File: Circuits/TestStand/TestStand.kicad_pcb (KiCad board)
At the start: 2 copper layers, 72.5 x 95 mm, 53 parts, among them J1 Screw_Terminal_01x07, J10 Screw_Terminal_01x03, J11 Screw_Terminal_01x03, J12 Screw_Terminal_01x03, J13 Screw_Terminal_01x03, J2 Screw_Terminal_01x07, J3 Screw_Terminal_01x07, J4 Screw_Terminal_01x03, J5 Screw_Terminal_01x03, J6 Screw_Terminal_01x03, J7 Screw_Terminal_01x03, J8 Screw_Terminal_01x03, J9 Screw_Terminal_01x03, Q1 MMBT4403-7-F, Q2 MMBT4403-7-F, Q3 MMBT4403-7-F, U1 HX711, U2 HX711, U3 HX711, U4 Teensy4.1

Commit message: did some traces
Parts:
- added C13: 0.01uF, Capacitor_SMD:C_0805_2012Metric, F.Cu at (98.5, 92.5)
- added C14: 10uF, Capacitor_SMD:C_0805_2012Metric, F.Cu at (92.5, 99.5)
- added C15: 10uF, Capacitor_SMD:C_0805_2012Metric, F.Cu at (92.5, 102.0)
- added C16: 33nF, Capacitor_SMD:C_0805_2012Metric, F.Cu at (71.5, 91.7)
- added C17: 22pF, Capacitor_SMD:C_0805_2012Metric, F.Cu at (85.0, 87.7)
- added C18: 22pF, Capacitor_SMD:C_0805_2012Metric, F.Cu at (85.0, 89.7)
- added C19: 2.2uF, Capacitor_SMD:C_0805_2012Metric, F.Cu at (78.0, 82.7)
- added C20: 4.7pF, Capacitor_SMD:C_0805_2012Metric, F.Cu at (78.0, 85.2)
- added C21: 1.5pF, Capacitor_SMD:C_0805_2012Metric, F.Cu at (72.5, 76.2)
- added C22: 1pF, Capacitor_SMD:C_0805_2012Metric, F.Cu at (76.0, 74.2)
- added C23: 10uF, Capacitor_SMD:C_0805_2012Metric, F.Cu at (66.5, 82.7)
- added C24: 10nF, Capacitor_SMD:C_0805_2012Metric, F.Cu at (66.5, 85.2)
- added C25: 1nF, Capacitor_SMD:C_0805_2012Metric, F.Cu at (66.5, 87.7)
- added D1: 1N4148, Diode_THT:D_DO-35_SOD27_P7.62mm_Horizontal, F.Cu at (96.5, 115.6)
- added D2: 1N4148, Diode_THT:D_DO-35_SOD27_P7.62mm_Horizontal, F.Cu at (100.0, 115.6)
- added FB1: FerriteBead, Inductor_SMD:L_0805_2012Metric, F.Cu at (97.5, 88.5)
- added FB2: FerriteBead, Inductor_SMD:L_0805_2012Metric, F.Cu at (99.5, 88.5)
- added J14: Screw_Terminal_01x02, Connector_Wago:Wago_734-132_1x02_P3.50mm_Vertical, F.Cu at (110.0, 90.0)
- added J15: Conn_Coaxial, Connector_Coaxial:SMA_Molex_73251-1153_EdgeMount_Horizontal, F.Cu at (72.5, 69.0)
- added L4: 2.7nH, Inductor_SMD:L_0805_2012Metric, F.Cu at (77.0, 79.7)
- added L5: 8.2nH, Inductor_SMD:L_0805_2012Metric, F.Cu at (76.0, 76.7)
- added L6: 3.9nH, Inductor_SMD:L_0805_2012Metric, F.Cu at (73.5, 79.1)
- added R16: 10k, Resistor_SMD:R_0805_2012Metric, F.Cu at (96.5, 105.5)
- added R17: 10k, Resistor_SMD:R_0805_2012Metric, F.Cu at (100.0, 105.5)
- added R18: 22k, Resistor_SMD:R_0805_2012Metric, F.Cu at (71.5, 87.7)
- added R19: 1M, Resistor_SMD:R_0805_2012Metric, F.Cu at (80.0, 88.8)
- added U5: LP2980IM5X-3.3/NOPB, Library:MF05A_TEX, F.Cu at (92.5, 95.7)
- added U6: MAX31855KASA, Package_SO:SOIC-8_3.9x4.9mm_P1.27mm, F.Cu at (98.5, 99.5)
- added U7: NRF24L01, Package_DFN_QFN:QFN-20-1EP_4x4mm_P0.5mm_EP2.5x2.5mm, F.Cu at (75.5, 89.6)
- added U8: LP2980IM5X-3.3/NOPB, Library:MF05A_TEX, F.Cu at (66.5, 91.4)
- added Y1: 16Mhz, Crystal:Crystal_SMD_2012-2Pin_2.0x1.2mm, F.Cu at (82.0, 88.7)
- moved J10 20.5 mm to (110.0, 145.9)
- moved J11 20.5 mm to (110.0, 131.9)
- moved J12 20.5 mm to (110.0, 118.0)
- moved J13 20.5 mm to (110.0, 104.0)
- moved J9 20.5 mm to (110.0, 160.0)
- moved J4 9.84 mm to (36.0, 168.5)
- moved J5 9.84 mm to (50.5, 168.5)
- moved J6 9.84 mm to (65.0, 168.5)
- moved J7 9.84 mm to (79.5, 168.5)
- moved J8 9.84 mm to (94.0, 168.5)
- moved U4 5.44 mm to (75.9, 130.7)
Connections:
- U4 pad 18: unconnected-(U4-26_A12_MOSI1-Pad18) -> /rMOSI
- U4 pad 19: unconnected-(U4-27_A13_SCK1-Pad19) -> /rSCK
- U4 pad 20: unconnected-(U4-28_RX7-Pad20) -> /rCE
- U4 pad 21: unconnected-(U4-29_TX7-Pad21) -> /rIRQ
- U4 pad 25: unconnected-(U4-33_MCLK2-Pad25) -> /tcCS
- U4 pad 26: unconnected-(U4-34_RX8-Pad26) -> /tcSO
- U4 pad 27: unconnected-(U4-35_TX8-Pad27) -> /tcSCK
- U4 pad 30: unconnected-(U4-38_CS1_IN1-Pad30) -> /rCSN
- U4 pad 31: unconnected-(U4-39_MISO1_OUT1A-Pad31) -> /rMISO
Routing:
- net GND: track 23.6 -> 106.7 mm, vias 4 -> 25
- net /PWM0: track 0.00 -> 62.6 mm
- net /PWM4: track 0.00 -> 56.5 mm
- net /PWM1: track 0.00 -> 54.1 mm
- net /tcSO: track 0.00 -> 52.8 mm
- net /PWM3: track 0.00 -> 52.6 mm
- net /tcCS: track 0.00 -> 49.6 mm
- net /PWM2: track 0.00 -> 45.6 mm
- net /+3VRF: track 0.00 -> 44.4 mm, vias 0 -> 2
- net /PT0: track 0.00 -> 41.0 mm
- net /B2+: track 0.00 -> 38.5 mm
- net /DAT2: track 0.00 -> 37.1 mm
- net /B1+: track 0.00 -> 37.0 mm
- net /SCK2: track 0.00 -> 36.0 mm
- net /PT1: track 0.00 -> 33.3 mm
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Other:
- board size 72.5 x 95 mm -> 92.5 x 111 mm

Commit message: added glow plug circuitry to schematic
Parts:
- added IC1: STP85NF55, Library:TO255P460X1020X2008-3P, F.Cu at (152.1, 96.5)
- added J16: Screw_Terminal_01x02, Connector_Wago:Wago_734-132_1x02_P3.50mm_Vertical, F.Cu at (152.5, 104.0)
- added R20: 10K, Resistor_SMD:R_0805_2012Metric, F.Cu at (158.5, 115.0)
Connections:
- U4 pad 13: unconnected-(U4-11_MOSI_CTX1-Pad13) -> /GP

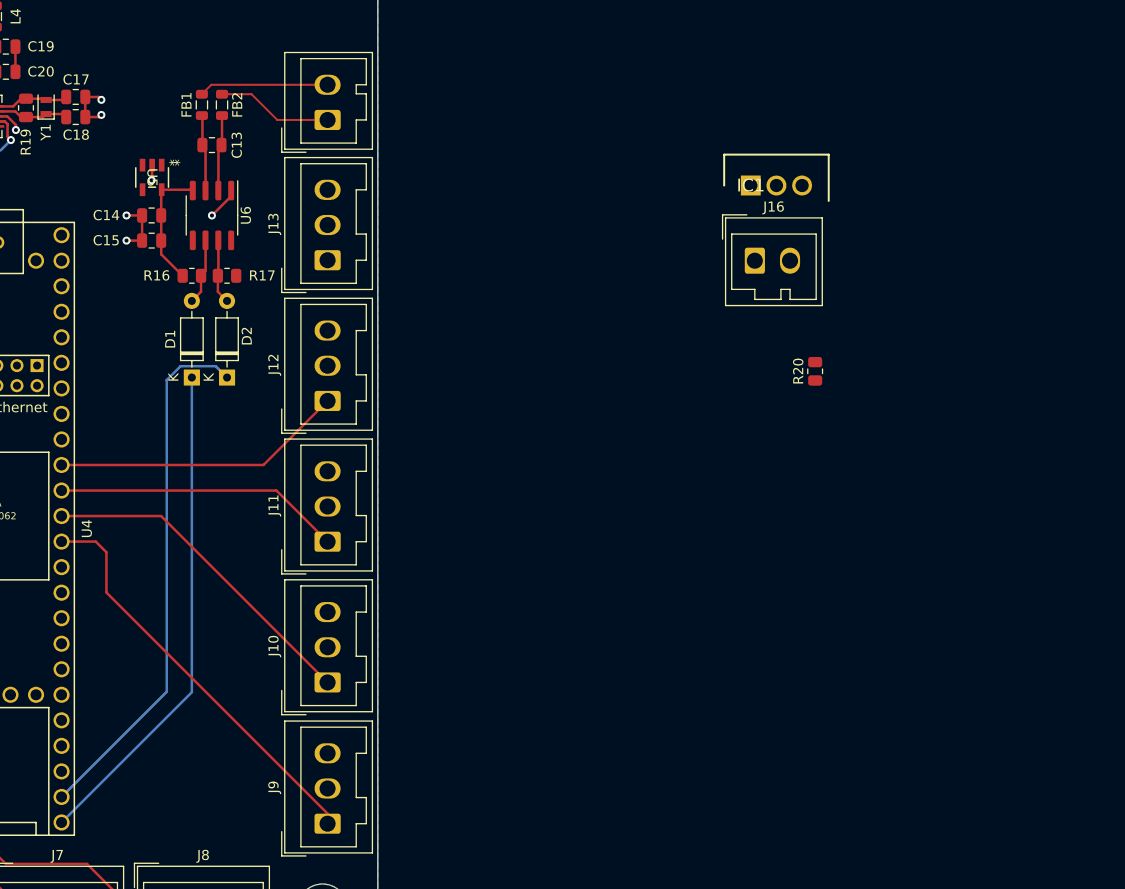
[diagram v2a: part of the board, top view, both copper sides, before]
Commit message: added voltage regulator stuff
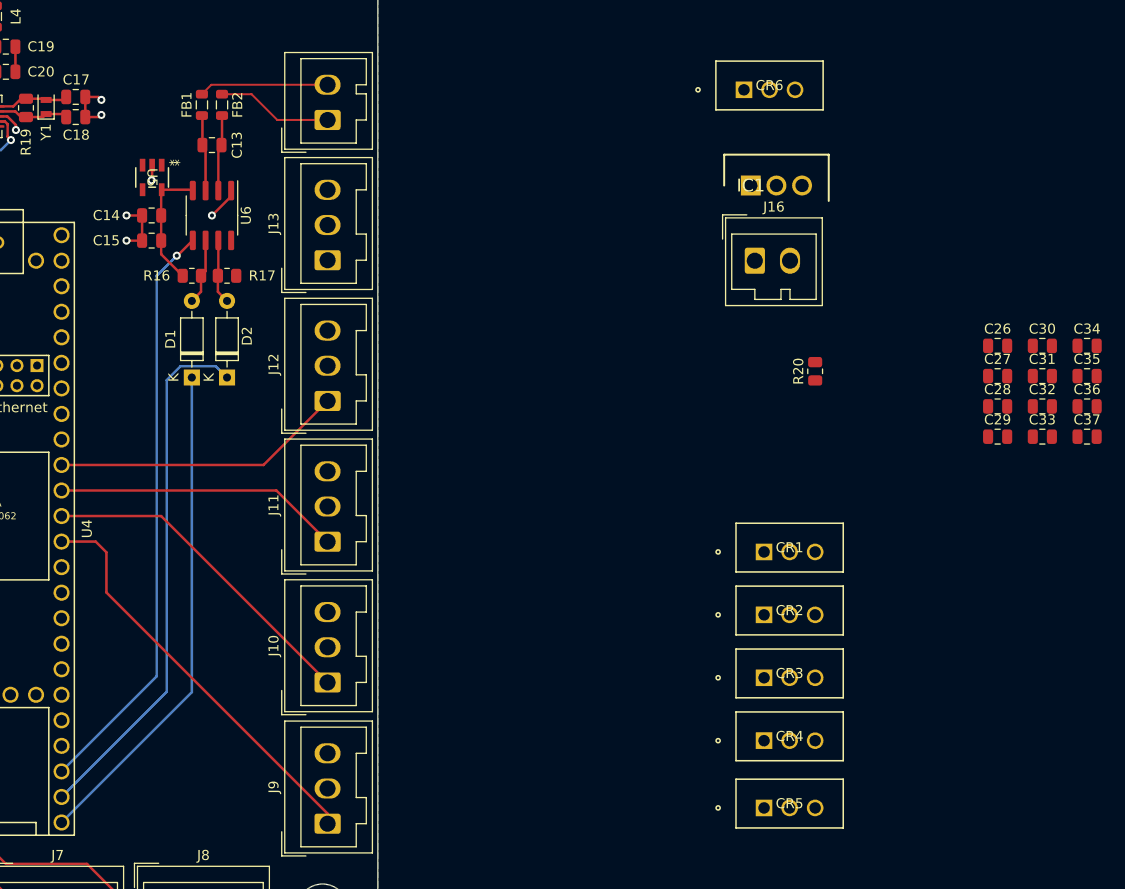
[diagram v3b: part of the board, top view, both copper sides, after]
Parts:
- added C26: 10uF, Capacitor_SMD:C_0805_2012Metric, F.Cu at (176.7, 112.5)
- added C27: 10uF, Capacitor_SMD:C_0805_2012Metric, F.Cu at (176.7, 115.5)
- added C28: 10uF, Capacitor_SMD:C_0805_2012Metric, F.Cu at (176.7, 118.5)
- added C29: 10uF, Capacitor_SMD:C_0805_2012Metric, F.Cu at (176.7, 121.5)
- added C30: 10uF, Capacitor_SMD:C_0805_2012Metric, F.Cu at (181.1, 112.5)
- added C31: 10uF, Capacitor_SMD:C_0805_2012Metric, F.Cu at (181.1, 115.5)
- added C32: 10uF, Capacitor_SMD:C_0805_2012Metric, F.Cu at (181.1, 118.5)
- added C33: 10uF, Capacitor_SMD:C_0805_2012Metric, F.Cu at (181.1, 121.5)
- added C34: 10uF, Capacitor_SMD:C_0805_2012Metric, F.Cu at (185.6, 112.5)
- added C35: 10uF, Capacitor_SMD:C_0805_2012Metric, F.Cu at (185.6, 115.5)
- added C36: 10uF, Capacitor_SMD:C_0805_2012Metric, F.Cu at (185.6, 118.5)
- added C37: 10uF, Capacitor_SMD:C_0805_2012Metric, F.Cu at (185.6, 121.5)
- added CR1: LD1085V50, Library:TO-220_STM, F.Cu at (153.4, 133.0)
- added CR2: LD1085V50, Library:TO-220_STM, F.Cu at (153.4, 139.2)
- added CR3: LD1085V50, Library:TO-220_STM, F.Cu at (153.4, 145.5)
- added CR4: LD1085V50, Library:TO-220_STM, F.Cu at (153.4, 151.7)
- added CR5: LD1085V50, Library:TO-220_STM, F.Cu at (153.4, 158.4)
- added CR6: LD1085V50, Library:TO-220_STM, F.Cu at (151.4, 87.0)
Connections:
- J16 pad 2: +12V -> +BATT
- J4 pad 2: +7.5V -> /+S0
- J5 pad 2: +7.5V -> /+S1
- J6 pad 2: +7.5V -> /+S2
- J7 pad 2: +7.5V -> /+S3
- J8 pad 2: +7.5V -> /+S4
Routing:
- net /tcSCK: track 0.00 -> 58.3 mm, vias 0 -> 1

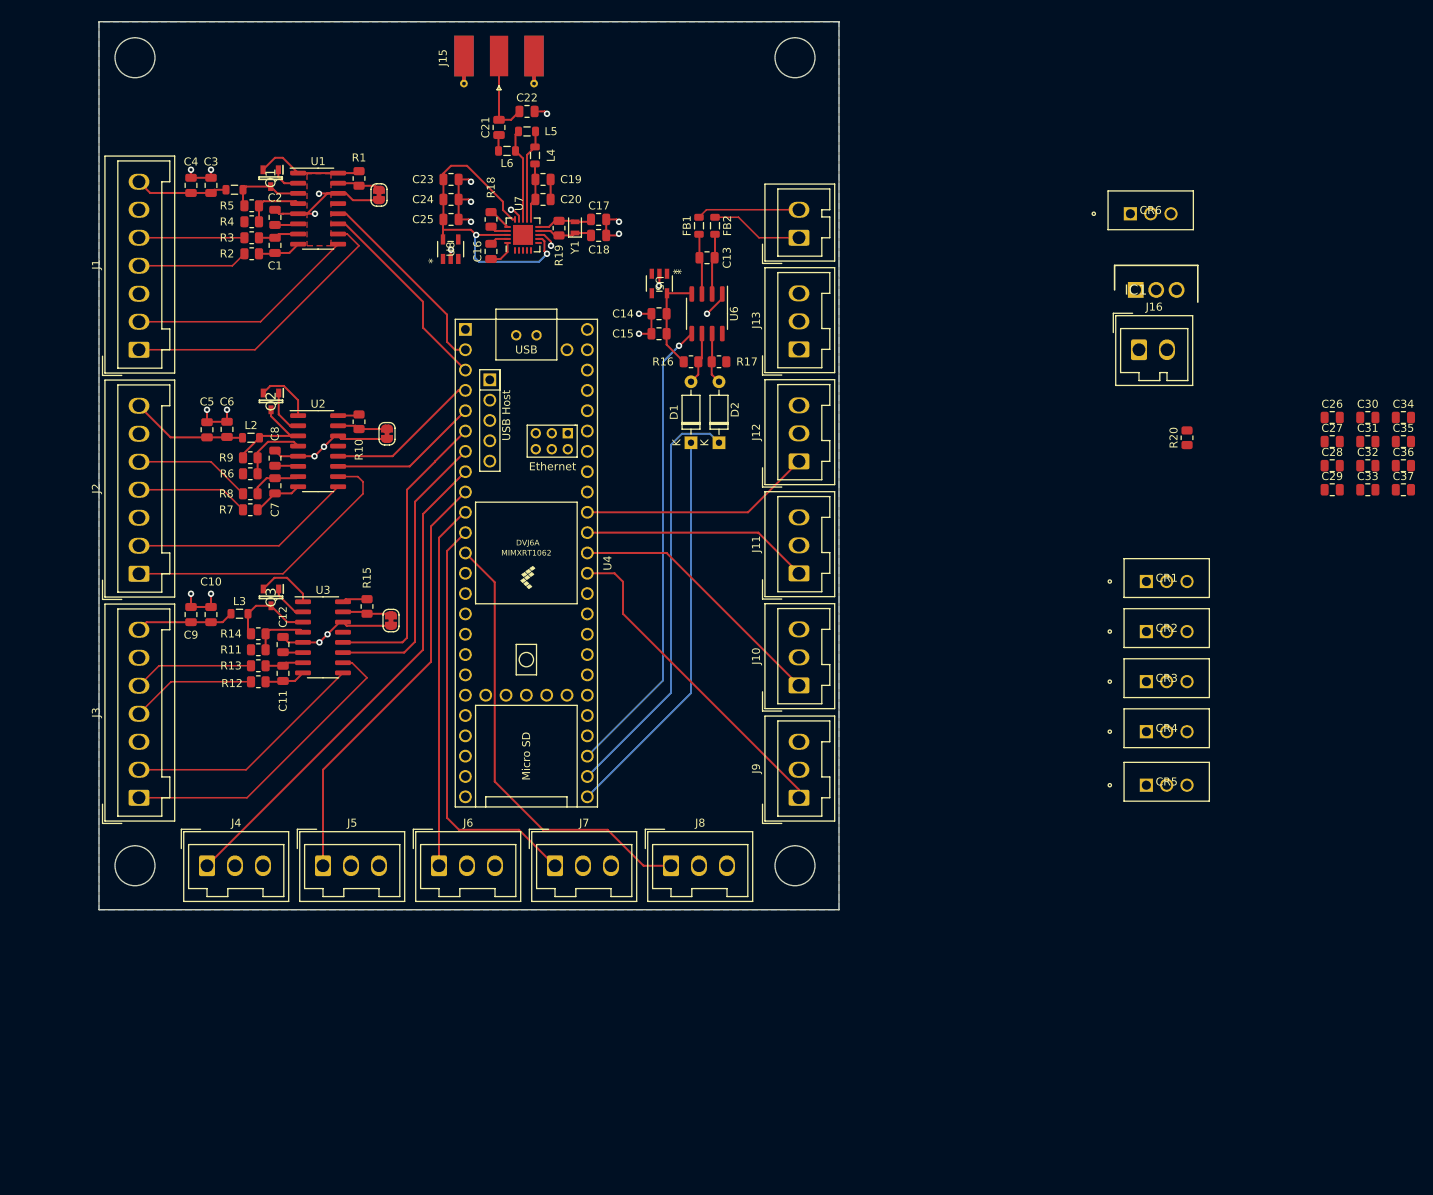
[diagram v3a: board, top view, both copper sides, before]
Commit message: Lots of tracing, filleting board shape
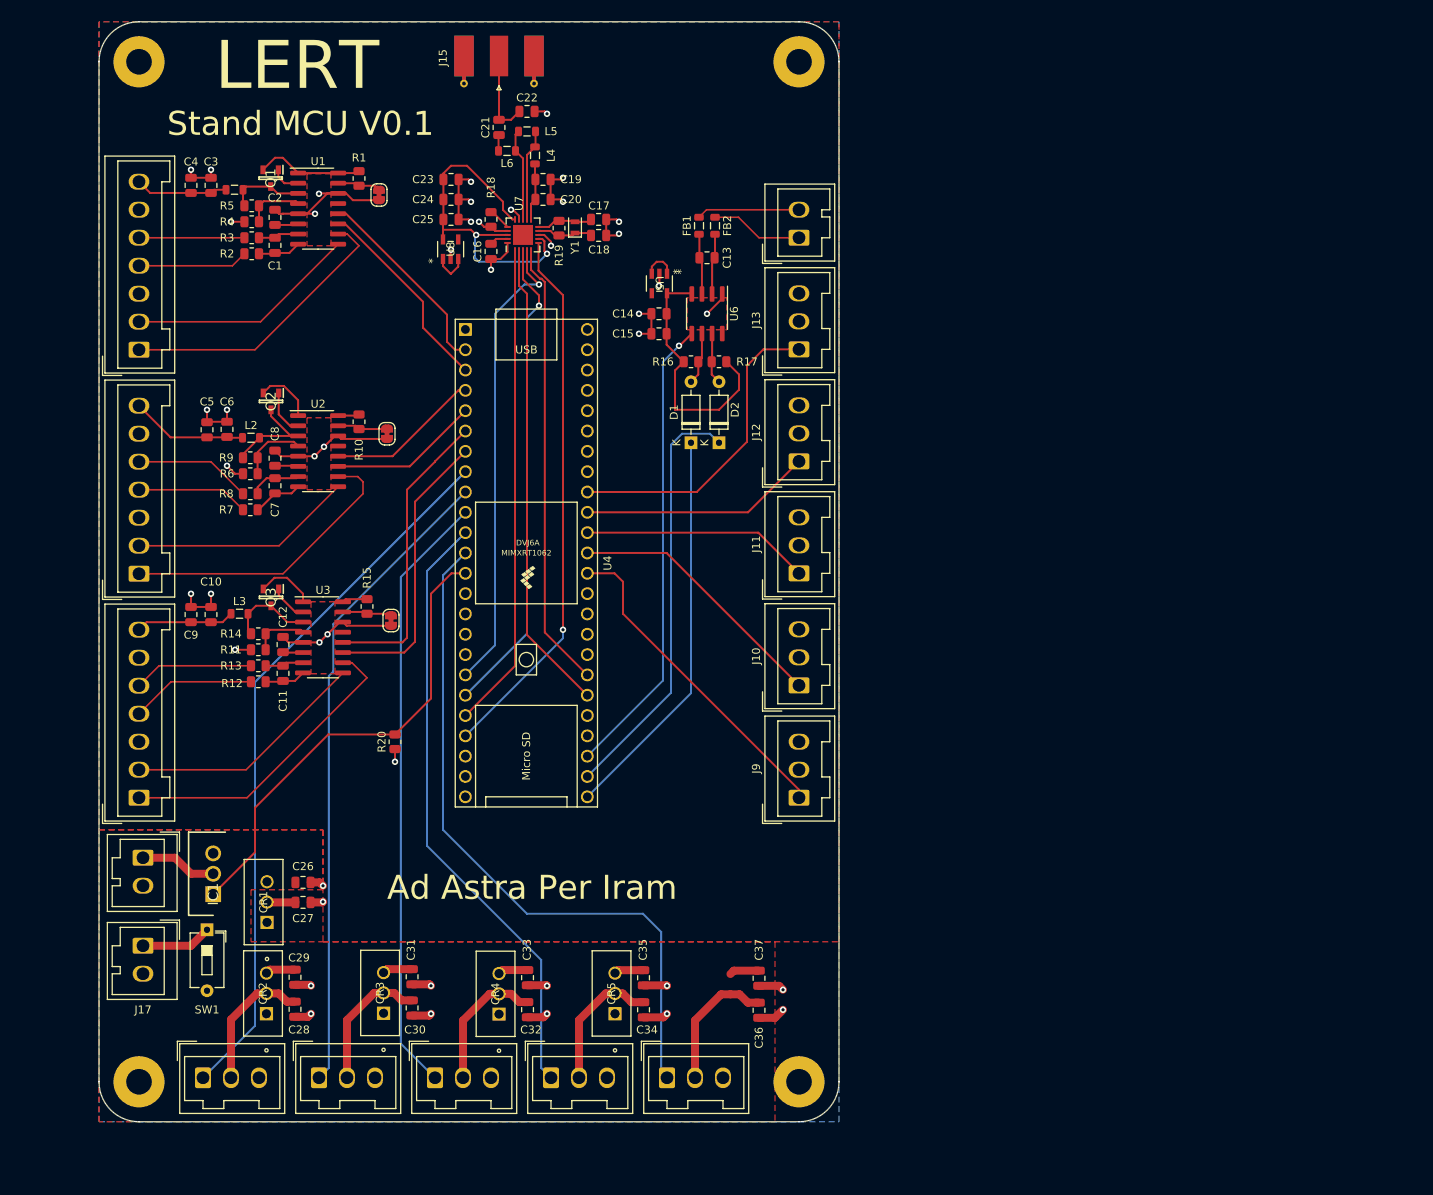
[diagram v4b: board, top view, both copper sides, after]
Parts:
- removed CR6: LD1085V50, Library:TO-220_STM
- added H1: MountingHole_Pad, MountingHole:MountingHole_3.2mm_M3_Pad, F.Cu at (27.5, 68.0)
- added H2: MountingHole_Pad, MountingHole:MountingHole_3.2mm_M3_Pad, F.Cu at (110.0, 68.0)
- added H3: MountingHole_Pad, MountingHole:MountingHole_3.2mm_M3_Pad, F.Cu at (110.0, 195.5)
- added H4: MountingHole_Pad, MountingHole:MountingHole_3.2mm_M3_Pad, F.Cu at (27.5, 195.5)
- added J17: Screw_Terminal_01x02, Connector_Wago:Wago_734-132_1x02_P3.50mm_Vertical, F.Cu at (28.0, 178.5)
- added SW1: SW_DIP_x01, Button_Switch_THT:SW_DIP_SPSTx01_Slide_6.7x4.1mm_W7.62mm_P2.54mm_LowProfile, F.Cu at (36.0, 176.5)
- moved C28 146.4 mm to (47.0, 186.4), turned to 90 degrees
- moved C29 143.3 mm to (47.0, 182.4), turned to 90 degrees
- moved C26 141.2 mm to (48.0, 170.6), turned to 180 degrees
- moved C27 141.0 mm to (48.0, 173.1), turned to 180 degrees
- moved C30 140.4 mm to (61.6, 186.3), turned to 90 degrees
- moved J16 139.8 mm to (28.0, 167.5), turned to -90 degrees
- moved IC1 137.9 mm to (36.8, 172.1), turned to 90 degrees
- moved C31 136.9 mm to (61.6, 182.4), turned to 90 degrees
- moved C32 125.1 mm to (76.1, 186.5), turned to 90 degrees
- moved C33 121.5 mm to (76.1, 182.5), turned to 90 degrees
- moved C34 120.4 mm to (90.6, 186.5), turned to 90 degrees
- moved CR2 119.9 mm to (43.4, 187.0), turned to 90 degrees
- moved CR1 117.9 mm to (43.5, 175.6), turned to 90 degrees
- moved C35 116.2 mm to (90.6, 182.5), turned to 90 degrees
- moved R20 106.0 mm to (59.5, 153.0)
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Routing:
- net /rIRQ: track 0.00 -> 67.9 mm, vias 0 -> 1
- net /rCE: track 0.00 -> 60.7 mm
- net /rSCK: track 0.00 -> 60.2 mm, vias 0 -> 1
- net /rCSN: track 0.00 -> 59.1 mm
- net /GP: track 0.00 -> 59.1 mm
- net /rMOSI: track 0.00 -> 58.6 mm, vias 0 -> 1
- net /rMISO: track 0.00 -> 56.1 mm
- net GND: track 106.7 -> 150.9 mm, vias 25 -> 45
- net /PT4: track 0.00 -> 39.4 mm
- net /PWM4: track 56.5 -> 86.9 mm
- net /PWM2: track 45.6 -> 75.9 mm
- net /PWM1: track 54.1 -> 80.8 mm
- net /PWM0: track 62.6 -> 89.3 mm
- net /PWM3: track 52.6 -> 76.5 mm
- net /+3VTC: track 12.6 -> 32.2 mm
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- added copper zone on F.Cu, net +5V
- added copper zone on F.Cu, net +BATT
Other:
- board size 92.5 x 111 mm -> 92.5 x 137.5 mm
- board text added: "Ad Astra Per Iram"
- board text added: "LERT"
- board text added: "Stand MCU V0.1"

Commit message: started generating some gerbers
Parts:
- added CR6: LD1085V50, Library:TO-220_STM, F.Cu at (101.5, 187.1)
